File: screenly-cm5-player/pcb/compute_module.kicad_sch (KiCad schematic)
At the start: 1 part, among them U1 CM5104064

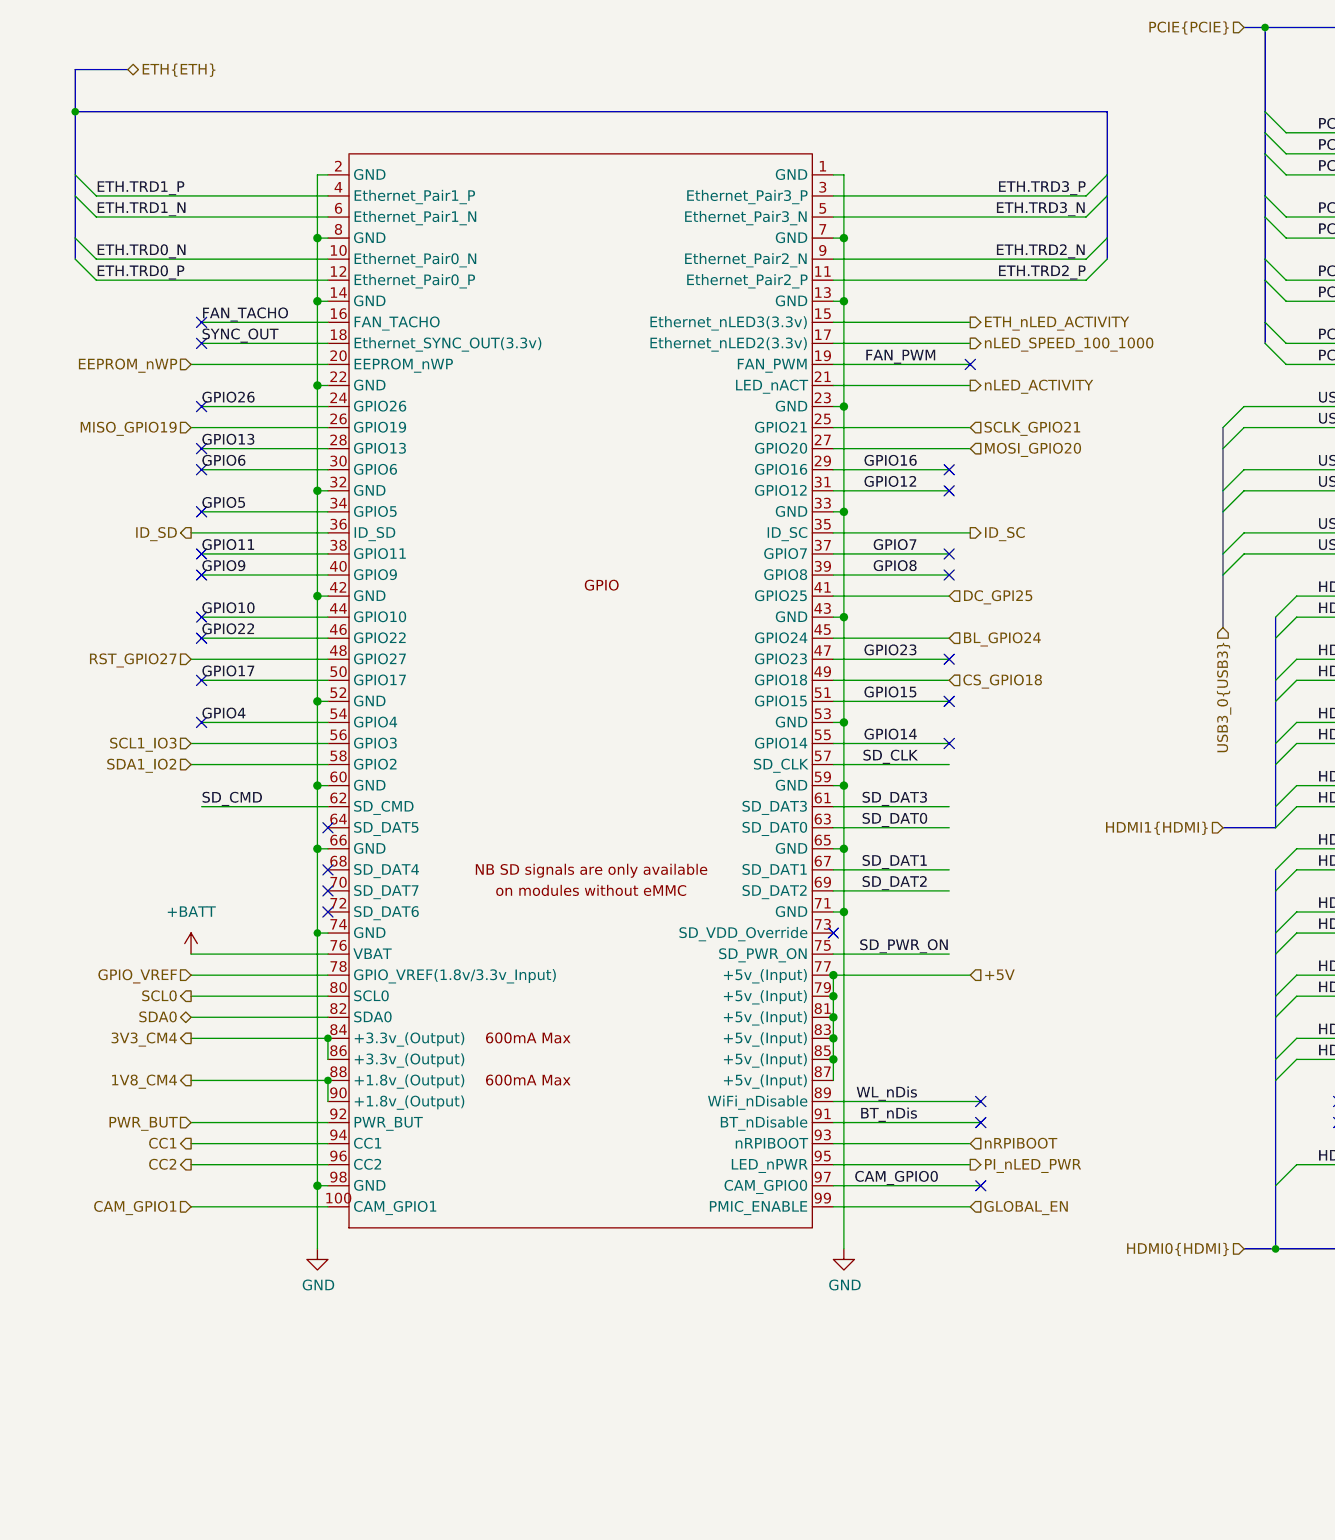
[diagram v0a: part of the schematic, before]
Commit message: Power stage completed
All power stage has been completed. It has 3 different controlled
outputs USB and PCIe power are separated from the main power due to
safety, durability and cost reasons. PCIe will be DNP later.
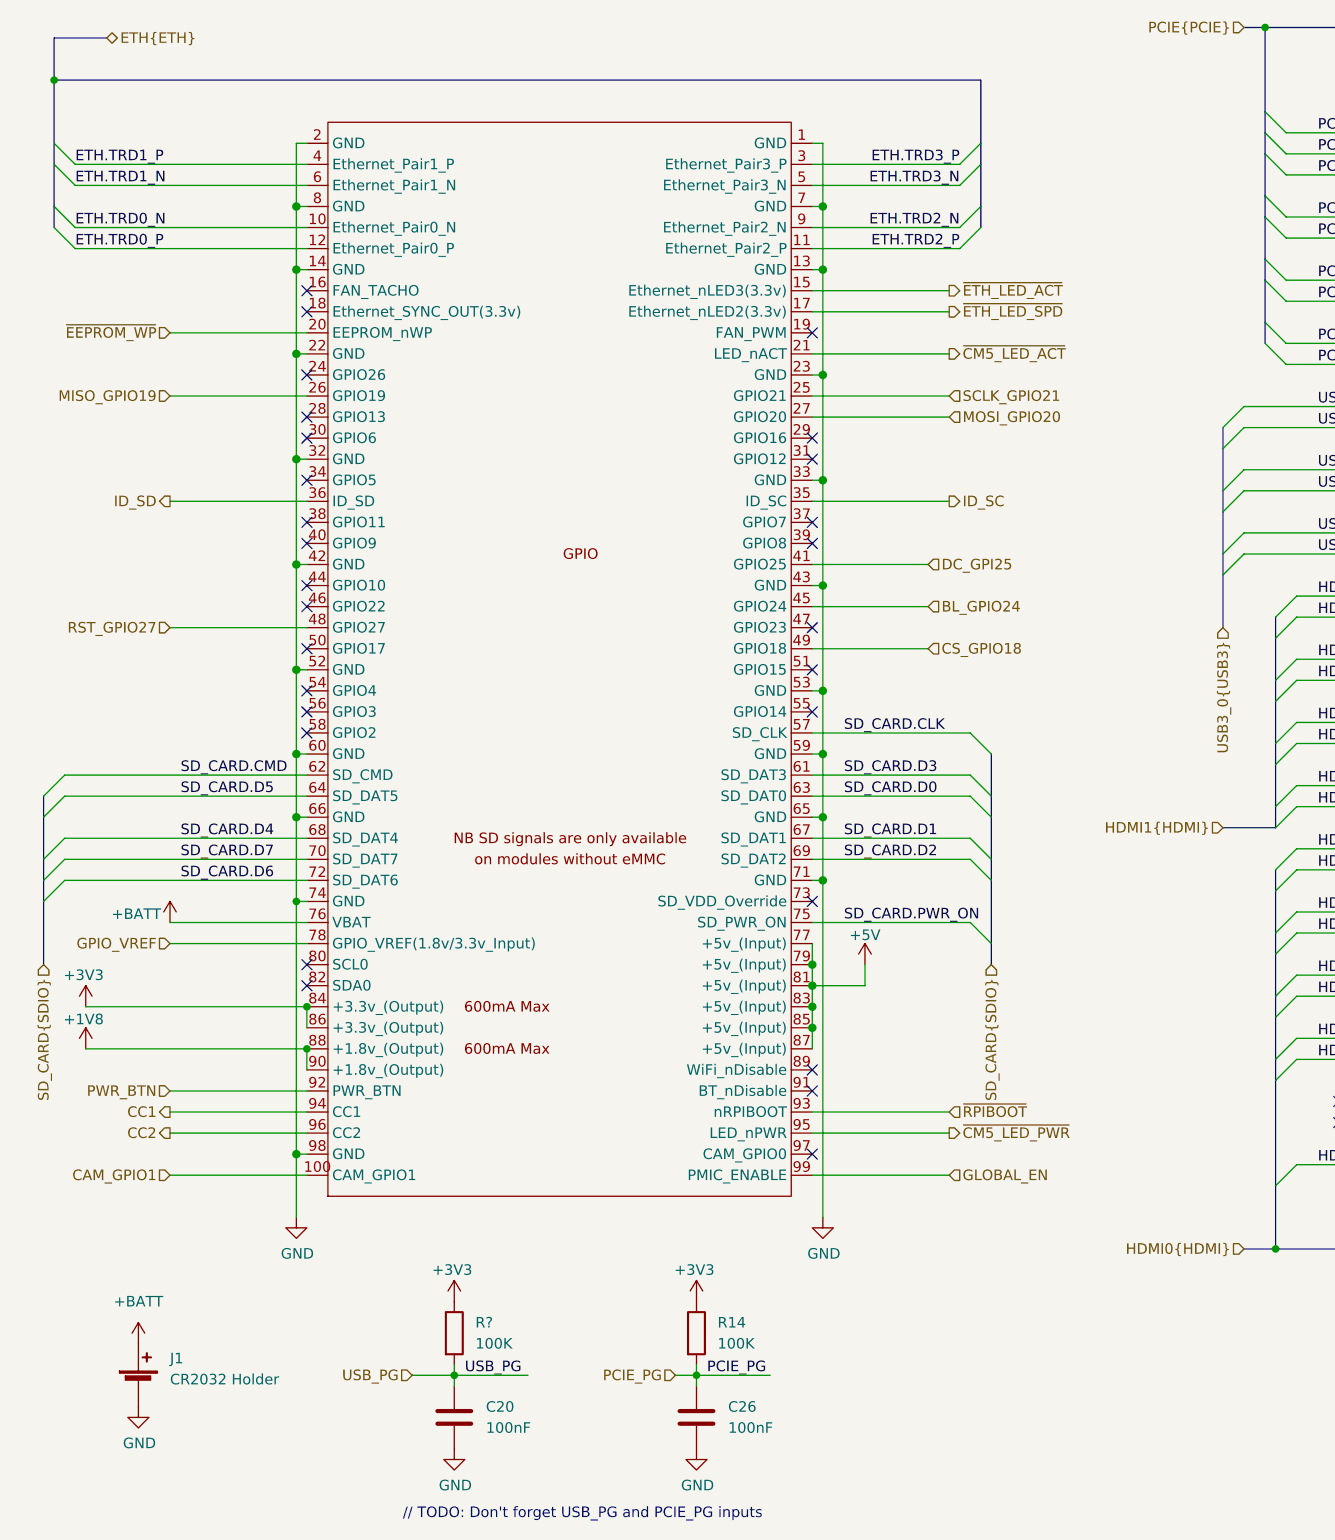
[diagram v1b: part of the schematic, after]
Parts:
- added C20, C26: 100nF, Screenly:C_0402, symbol Screenly:Capacitor 100nF 50V X7R 0402 (CL05B104KB54PNC)
- added J1: CR2032 Holder, Screenly:BatteryHolder_MYOUNG_BS-02_CR2032, symbol Screenly:Battery Holder CR2032 THT (BS-02-A1AJ010)
- added R14, R?: 100K, Screenly:R_0402, symbol Screenly:Resistor 100K 1% 0402 (0402WGF1003TCE)
- U1: Manufacturer (none) -> Raspberry Pi; MfrPartNum (none) -> CM5104064; PartNumber (none) -> SRLY-MOD-000001; temp_max (none) -> 85C; temp_min (none) -> -20C
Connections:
- net +BATT: now also J1.1 (+)
- net GND: now also C20.1, C26.1, J1.2 (-)
- net SD_CARD.D5: now reaches U1.64 (SD_DAT5)
- net SD_CARD.D4: now reaches U1.68 (SD_DAT4)
- net SD_CARD.D7: now reaches U1.70 (SD_DAT7)
- net SD_CARD.D6: now reaches U1.72 (SD_DAT6)
- net 1V8_CM4 renamed +1V8
- net 3V3_CM4 renamed +3V3
- net +3V3: now also R14.1, R?.1
- net BT_nDis: no longer names the net of U1.91 (BT_nDisable)
- net CAM_GPIO0: no longer names the net of U1.97 (CAM_GPIO0)
- net EEPROM_nWP renamed ~{EEPROM_WP}
- net ETH_nLED_ACTIVITY renamed ~{ETH_LED_ACT}
- net FAN_PWM: no longer names the net of U1.19 (FAN_PWM)
- net FAN_TACHO: no longer names the net of U1.16 (FAN_TACHO)
- net GPIO10: no longer names the net of U1.44 (GPIO10)
- net GPIO11: no longer names the net of U1.38 (GPIO11)
- net GPIO12: no longer names the net of U1.31 (GPIO12)
- net GPIO13: no longer names the net of U1.28 (GPIO13)
- net GPIO14: no longer names the net of U1.55 (GPIO14)
- net GPIO15: no longer names the net of U1.51 (GPIO15)
- net GPIO16: no longer names the net of U1.29 (GPIO16)
- net GPIO17: no longer names the net of U1.50 (GPIO17)
- net GPIO22: no longer names the net of U1.46 (GPIO22)
- net GPIO23: no longer names the net of U1.47 (GPIO23)
- net GPIO26: no longer names the net of U1.24 (GPIO26)
- net GPIO4: no longer names the net of U1.54 (GPIO4)
- net GPIO5: no longer names the net of U1.34 (GPIO5)
- net GPIO6: no longer names the net of U1.30 (GPIO6)
- net GPIO7: no longer names the net of U1.37 (GPIO7)
- net GPIO8: no longer names the net of U1.39 (GPIO8)
- net GPIO9: no longer names the net of U1.40 (GPIO9)
- net PI_nLED_PWR renamed ~{CM5_LED_PWR}
- net PWR_BUT renamed PWR_BTN
- net SCL0: no longer names the net of U1.80 (SCL0)
- net SCL1_IO3: no longer names the net of U1.56 (GPIO3)
- net SDA0: no longer names the net of U1.82 (SDA0)
- net SDA1_IO2: no longer names the net of U1.58 (GPIO2)
- net SD_CLK renamed SD_CARD.CLK
- net SD_CMD renamed SD_CARD.CMD
- net SD_DAT0 renamed SD_CARD.D0
- net SD_DAT1 renamed SD_CARD.D1
- net SD_DAT2 renamed SD_CARD.D2
- net SD_DAT3 renamed SD_CARD.D3
- net SD_PWR_ON renamed SD_CARD.PWR_ON
- net SYNC_OUT: no longer names the net of U1.18 (Ethernet_SYNC_OUT(3.3v))
- net WL_nDis: no longer names the net of U1.89 (WiFi_nDisable)
- net nLED_ACTIVITY renamed ~{CM5_LED_ACT}
- net nLED_SPEED_100_1000 renamed ~{ETH_LED_SPD}
- net nRPIBOOT renamed ~{RPIBOOT}
- new net PCIE_PG: C26.2, R14.2
- new net USB_PG: C20.2, R?.2
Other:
- note added: "// TODO: Don't forget USB_PG and PCIE_PG inputs"

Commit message: Ethernet and PCIe sections are done.
Modified power section and moved PCIe specific circuit into its own
section.
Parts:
- gave numbers to parts that had none: 1
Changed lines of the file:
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@@
 	)
 	(junction
-		(at 162.56 16.51)
+		(at 157.48 16.51)
 		(diameter 0)
 		(color 0 0 0 0)
@@
 	)
 	(bus_entry
-		(at 162.56 39.37)
+		(at 157.48 39.37)
 		(size 2.54 2.54)
 		(stroke
@@
 	)
 	(bus_entry
-		(at 162.56 29.21)
+		(at 157.48 29.21)
 		(size 2.54 2.54)
 		(stroke
@@
 	)
 	(bus_entry
-		(at 162.56 26.67)
+		(at 157.48 26.67)
 		(size 2.54 2.54)
 		(stroke
@@
 	)
 	(bus_entry
-		(at 162.56 31.75)
-		(size 2.54 2.54)
-		(stroke
-			(width 0)
-			(type default)
-		)
-	)
-	(bus_entry
 		(at 16.51 40.64)
 		(size 2.54 2.54)
@@
 	)
 	(bus_entry
-		(at 162.56 36.83)
+		(at 157.48 36.83)
 		(size 2.54 2.54)
 		(stroke
@@
 	)
 	(bus_entry
-		(at 162.56 54.61)
+		(at 157.48 54.61)
 		(size 2.54 2.54)
 		(stroke
@@
 	)
 	(bus_entry
+		(at 157.48 31.75)
+		(size 2.54 2.54)
+		(stroke
+			(width 0)
+			(type default)
+		)
+	)
+	(bus_entry
 		(at 163.83 87.63)
 		(size 2.54 -2.54)
@@
 	)
 	(bus_entry
-		(at 162.56 52.07)
+		(at 157.48 52.07)
 		(size 2.54 2.54)
 		(stroke
@@
 	)
 	(bus_entry
-		(at 162.56 46.99)
+		(at 157.48 46.99)
 		(size 2.54 2.54)
 		(stroke
@@
 	)
 	(bus_entry
-		(at 162.56 44.45)
+		(at 157.48 44.45)
 		(size 2.54 2.54)
 		(stroke
@@
 	(wire
 		(pts
-			(xy 165.1 41.91) (xy 187.96 41.91)
+			(xy 160.02 41.91) (xy 187.96 41.91)
 		)
 		(stroke
@@
 		)
 	)
-	(wire
-		(pts
-			(xy 165.1 34.29) (xy 187.96 34.29)
-		)
-		(stroke
-			(width 0)
-			(type default)
-		)
-	)
 	(bus
 		(pts
@@
 	(bus
 		(pts
-			(xy 162.56 36.83) (xy 162.56 31.75)
+			(xy 157.48 29.21) (xy 157.48 36.83)
 		)
 		(stroke
@@
 	(bus
 		(pts
-			(xy 162.56 39.37) (xy 162.56 36.83)
+			(xy 157.48 39.37) (xy 157.48 36.83)
 		)
 		(stroke
@@
 	(wire
 		(pts
-			(xy 165.1 46.99) (xy 187.96 46.99)
+			(xy 160.02 46.99) (xy 187.96 46.99)
 		)
 		(stroke
@@
 	(bus
 		(pts
-			(xy 162.56 54.61) (xy 162.56 52.07)
+			(xy 157.48 54.61) (xy 157.48 52.07)
 		)
 		(stroke
@@
 		)
 	)
-	(bus
-		(pts
-			(xy 162.56 31.75) (xy 162.56 29.21)
-		)
-		(stroke
-			(width 0)
-			(type default)
-		)
-	)
 	(wire
 		(pts
@@
 	(bus
 		(pts
-			(xy 162.56 29.21) (xy 162.56 26.67)
+			(xy 157.48 29.21) (xy 157.48 26.67)
 		)
 		(stroke
@@
 	(bus
 		(pts
-			(xy 162.56 44.45) (xy 162.56 39.37)
+			(xy 157.48 44.45) (xy 157.48 39.37)
 		)
 		(stroke
@@
 	(wire
 		(pts
-			(xy 165.1 29.21) (xy 187.96 29.21)
+			(xy 160.02 29.21) (xy 187.96 29.21)
 		)
 		(stroke
@@
 	(bus
 		(pts
-			(xy 269.24 16.51) (xy 162.56 16.51)
+			(xy 269.24 16.51) (xy 157.48 16.51)
 		)
 		(stroke
@@
 	(bus
 		(pts
-			(xy 162.56 52.07) (xy 162.56 46.99)
+			(xy 157.48 52.07) (xy 157.48 46.99)
 		)
 		(stroke
@@
 	(bus
 		(pts
-			(xy 160.02 16.51) (xy 162.56 16.51)
+			(xy 154.94 16.51) (xy 157.48 16.51)
 		)
 		(stroke
@@
 	(wire
 		(pts
-			(xy 165.1 57.15) (xy 187.96 57.15)
+			(xy 160.02 57.15) (xy 187.96 57.15)
 		)
 		(stroke
@@
 	(wire
 		(pts
-			(xy 165.1 54.61) (xy 187.96 54.61)
+			(xy 160.02 54.61) (xy 187.96 54.61)
 		)
 		(stroke
@@
 	(bus
 		(pts
-			(xy 162.56 16.51) (xy 162.56 26.67)
+			(xy 157.48 16.51) (xy 157.48 26.67)
 		)
 		(stroke
@@
 	(wire
 		(pts
-			(xy 165.1 39.37) (xy 187.96 39.37)
+			(xy 160.02 39.37) (xy 187.96 39.37)
 		)
 		(stroke
@@
 	(wire
 		(pts
-			(xy 165.1 49.53) (xy 187.96 49.53)
+			(xy 160.02 49.53) (xy 187.96 49.53)
 		)
 		(stroke
@@
 	(wire
 		(pts
+			(xy 160.02 34.29) (xy 187.96 34.29)
+		)
+		(stroke
+			(width 0)
+			(type default)
+		)
+	)
+	(wire
+		(pts
 			(xy 125.73 33.02) (xy 107.95 33.02)
 		)
@@
 	(bus
 		(pts
-			(xy 162.56 46.99) (xy 162.56 44.45)
+			(xy 157.48 46.99) (xy 157.48 44.45)
 		)
 		(stroke
@@
 	(wire
 		(pts
-			(xy 165.1 31.75) (xy 187.96 31.75)
+			(xy 160.02 31.75) (xy 187.96 31.75)
 		)
 		(stroke
@@
 		)
 	)
-	(label "PCIE.PWR_EN"
-		(at 168.91 34.29 0)
-		(effects
-			(font
-				(size 1.27 1.27)
-			)
-			(justify left bottom)
-		)
-	)
 	(label "HDMI0.D2_P"
 		(at 168.91 115.57 0)
@@
 		)
 	)
+	(label "PCIE.PWR_EN"
+		(at 168.91 34.29 0)
+		(effects
+			(font
+				(size 1.27 1.27)
+			)
+			(justify left bottom)
+		)
+	)
 	(label "PCIE.RX_N"
 		(at 168.91 49.53 0)
@@
 	)
 	(hierarchical_label "PCIE{PCIE}"
-		(shape input)
-		(at 160.02 16.51 180)
+		(shape output)
+		(at 154.94 16.51 180)
 		(effects
 			(font
@@
 		(dnp no)
 		(fields_autoplaced yes)
-		(property "Reference" "R?"
+		(property "Reference" "R15"
 			(at 67.31 172.7199 0)
 			(show_name no)
@@
 			(project "screenly-cm5-player"
 				(path "/e8a2875a-18ea-4799-b56d-ecb6ae09ef8e/3fbfb189-ea05-4055-8850-fa2523ec0120"
-					(reference "R?")
+					(reference "R15")
 					(unit 1)
 				)

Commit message: WIP Schematics
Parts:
- removed C20, C26: 100nF, Screenly:C_0402, symbol Screenly:Capacitor 100nF 50V X7R 0402 (CL05B104KB54PNC)
- removed R14, R15: 100K, Screenly:R_0402, symbol Screenly:Resistor 100K 1% 0402 (0402WGF1003TCE)
- added R14: 0, Screenly:SolderBridge_0402, symbol Screenly:Resistor 0R Jumper 0402 (0402WGF0000TCE)
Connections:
- net GPIO_VREF is gone; now on net +3V3: U1.78 (GPIO_VREF(1.8v/3.3v_Input))
- net GND: now also R14.1
- net BL_GPIO24: no longer names the net of U1.45 (GPIO24)
- net CS_GPIO18: no longer names the net of U1.49 (GPIO18)
- net DC_GPI25: no longer names the net of U1.41 (GPIO25)
- net ID_SC: no longer names the net of U1.35 (ID_SC)
- net ID_SD: no longer names the net of U1.36 (ID_SD)
- net RST_GPIO27: no longer names the net of U1.48 (GPIO27)
- net ~{EEPROM_WP}: no longer names the net of U1.20 (EEPROM_nWP)
- net ~{EEPROM_WP}: now also R14.2
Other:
- note removed: "// TODO: Don't forget USB_PG and PCIE_PG inputs"

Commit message: Revised USB design 1xUSB-C 2.0, 2xUSB-A 3.0
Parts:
- added R33: 120, Screenly:R_0402, symbol Screenly:Resistor 120R 5% 0402 (0402WGJ0121TCE)
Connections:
- net VBUS_EN: now also R33.2; no longer U1.111 (VBUS_EN)
- new net: R33.1, U1.111 (VBUS_EN)
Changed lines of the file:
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@@
 	(wire
 		(pts
+			(xy 262.89 41.91) (xy 267.97 41.91)
+		)
+		(stroke
+			(width 0)
+			(type default)
+		)
+	)
+	(wire
+		(pts
 			(xy 166.37 100.33) (xy 187.96 100.33)
 		)
@@
 	(hierarchical_label "VBUS_EN"
 		(shape output)
-		(at 255.27 41.91 0)
+		(at 267.97 41.91 0)
 		(effects
 			(font
@@
 					(unit 1)
 				)
+			)
+		)
+	)
+	(symbol
+		(lib_id "Screenly:Resistor 120R 5% 0402 (0402WGJ0121TCE)")
+		(at 259.08 41.91 90)
+		(unit 1)
+		(body_style 1)
+		(exclude_from_sim no)
+		(in_bom yes)
+		(on_board yes)
+		(in_pos_files yes)
+		(dnp no)
+		(property "Reference" "R33"
+			(at 254.254 40.894 90)
+			(show_name no)
+			(do_not_autoplace no)
+			(effects
+				(font
+					(size 1.27 1.27)
+				)
+			)
+		)
+		(property "Value" "120"
+			(at 259.08 41.91 90)
+			(show_name no)
+			(do_not_autoplace no)
+			(effects
+				(font
+					(size 1.27 1.27)
+				)
+			)
+		)
+		(property "Footprint" "Screenly:R_0402"
+			(at 259.08 43.688 90)
+			(hide yes)
+			(show_name no)
+			(do_not_autoplace no)
+			(effects
+				(font
+					(size 1.27 1.27)
+				)
+			)
+		)
+		(property "Datasheet" "https://www.lcsc.com/datasheet/C25530.pdf"
+			(at 259.08 41.91 0)
+			(hide yes)
+			(show_name no)
+			(do_not_autoplace no)
+			(effects
+				(font
+					(size 1.27 1.27)
+				)
+			)
+		)
+		(property "Description" "120 Ohm 5% 62.5mW 0402 thick film chip resistor"
+			(at 259.08 41.91 0)
+			(hide yes)
+			(show_name no)
+			(do_not_autoplace no)
+			(effects
+				(font
+					(size 1.27 1.27)
+				)
+			)
+		)
+		(property "PartNumber" "SRLY-RES-000009"
+			(at 259.08 41.91 0)
+			(hide yes)
+			(show_name no)
+			(do_not_autoplace no)
+			(effects
+				(font
+					(size 1.27 1.27)
+				)
+			)
+		)
+		(property "Manufacturer" "UNI-ROYAL"
+			(at 259.08 41.91 0)
+			(hide yes)
+			(show_name no)
+			(do_not_autoplace no)
+			(effects
+				(font
+					(size 1.27 1.27)
+				)
+			)
+		)
+		(property "MfrPartNum" "0402WGJ0121TCE"
+			(at 259.08 41.91 0)
+			(hide yes)
+			(show_name no)
+			(do_not_autoplace no)
+			(effects
+				(font
+					(size 1.27 1.27)
+				)
+			)
+		)
+		(property "tolerance" "5%"
+			(at 259.08 41.91 0)
+			(hide yes)
+			(show_name no)
+			(do_not_autoplace no)
+			(effects
+				(font
+					(size 1.27 1.27)
+				)
+			)
+		)
+		(property "power" "62.5mW"
+			(at 259.08 41.91 0)
+			(hide yes)
+			(show_name no)
+			(do_not_autoplace no)
+			(effects
+				(font
+					(size 1.27 1.27)
+				)
+			)
+		)
+		(property "voltage" "50V"
+			(at 259.08 41.91 0)
+			(hide yes)
+			(show_name no)
+			(do_not_autoplace no)
+			(effects
+				(font
+					(size 1.27 1.27)
+				)
+			)
+		)
+		(property "tempco" "100ppm"
+			(at 259.08 41.91 0)
+			(hide yes)
+			(show_name no)
+			(do_not_autoplace no)
+			(effects
+				(font
+					(size 1.27 1.27)
+				)
+			)
+		)
+		(property "technology" "thick_film"
+			(at 259.08 41.91 0)
+			(hide yes)
+			(show_name no)
+			(do_not_autoplace no)
+			(effects
+				(font
+					(size 1.27 1.27)
+				)
+			)
+		)
+		(property "temp_min" "-55C"
+			(at 259.08 41.91 0)
+			(hide yes)
+			(show_name no)
+			(do_not_autoplace no)
+			(effects
+				(font
+					(size 1.27 1.27)
+				)
+			)
+		)
+		(property "temp_max" "155C"
+			(at 259.08 41.91 0)
+			(hide yes)
+			(show_name no)
+			(do_not_autoplace no)
+			(effects
+				(font
+					(size 1.27 1.27)
+				)
+			)
+		)
+		(pin "1"
+		)
+		(pin "2"
+		)
+		(instances
+			(project "screenly-cm5-player"
+				(path "/e8a2875a-18ea-4799-b56d-ecb6ae09ef8e/3fbfb189-ea05-4055-8850-fa2523ec0120"
+					(reference "R33")
+					(unit 1)
+				)
